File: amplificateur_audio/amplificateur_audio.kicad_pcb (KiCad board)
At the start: 2 copper layers, 54 parts, among them J2 Conn_01x02, J3 Conn_01x03, K1 Relay_1CT, Q1 Q_PNP_EBC, Q10 Q_PNP_BCE, Q11 BC636, Q12 Q_NPN_BCE, Q13 Q_NPN_EBC, Q2 Q_PNP_EBC, Q3 Q_PNP_EBC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

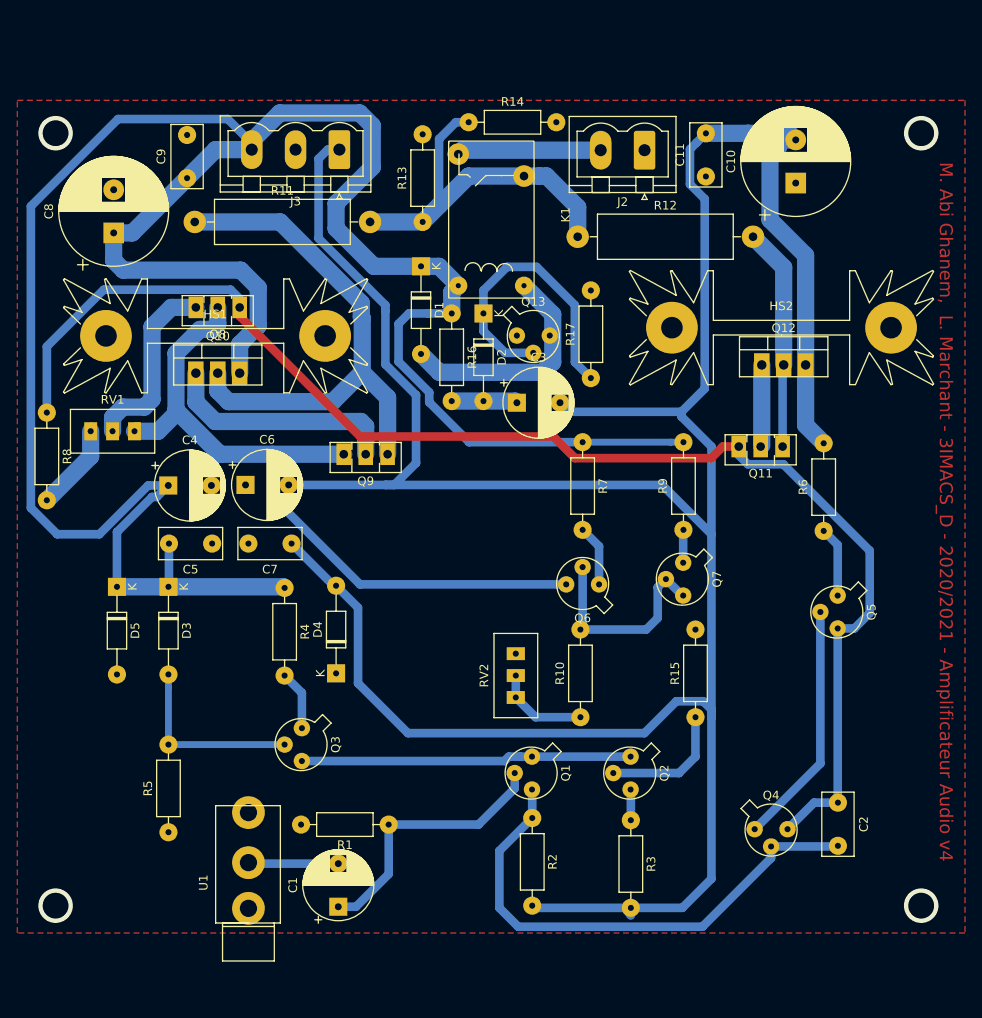
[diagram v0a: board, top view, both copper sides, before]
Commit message: ajout de plan de masse back + vias entre les plans de masses
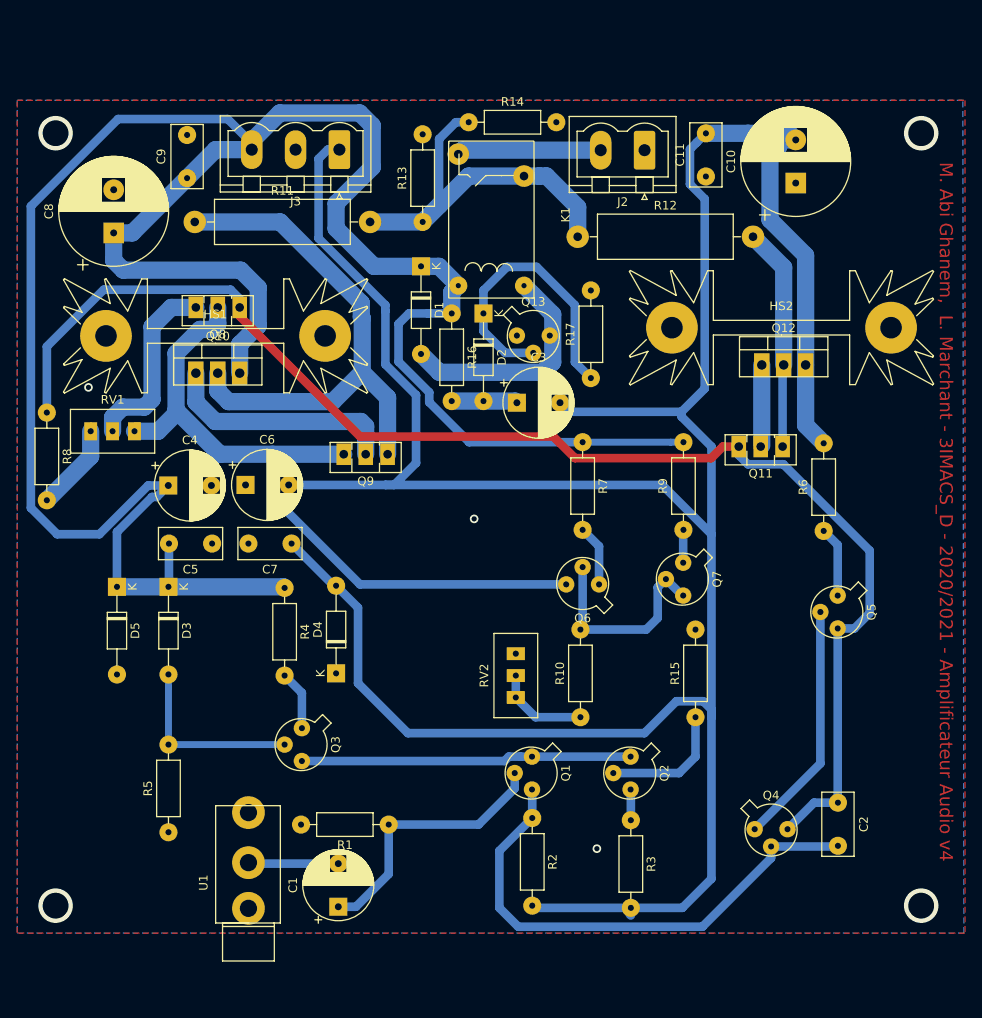
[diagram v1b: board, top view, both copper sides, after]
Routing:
- net GND: vias 0 -> 3
- added copper zone on B.Cu, net GND
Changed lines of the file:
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@@
     (thickness 1.6)
     (drawings 10)
-    (tracks 279)
+    (tracks 282)
     (zones 0)
     (modules 54)
@@
   )
   (setup
-    (last_trace_width 0.7)
+    (last_trace_width 1)
     (user_trace_width 0.8)
     (user_trace_width 1)
@@
   (segment (start 69.064621 99.441) (end 64.1784 94.554779) (width 1) (layer B.Cu) (net 6))
   (segment (start 69.342 99.441) (end 69.064621 99.441) (width 1) (layer B.Cu) (net 6))
+  (via (at 85.344 91.694) (size 1) (drill 0.6) (layers F.Cu B.Cu) (net 7))
+  (via (at 99.568 129.921) (size 1) (drill 0.6) (layers F.Cu B.Cu) (net 7))
+  (via (at 40.64 76.454) (size 1) (drill 0.6) (layers F.Cu B.Cu) (net 7))
   (segment (start 55.372 48.895) (end 52.07 52.197) (width 2) (layer B.Cu) (net 8))
   (segment (start 59.563 48.895) (end 55.372 48.895) (width 2) (layer B.Cu) (net 8))
@@
       )
     )
+  )
+  (zone (net 7) (net_name GND) (layer B.Cu) (hatch edge 0.508)
+    (connect_pads (clearance 0.508))
+    (min_thickness 0.254)
+    (fill yes (arc_segments 16) (thermal_gap 0.508) (thermal_bridge_width 0.508))
+    (polygon
+      (pts
+        (xy 32.385 43.18) (xy 32.385 139.7) (xy 142.113 139.7) (xy 141.986 43.18)
+      )
+    )

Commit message: ampli audio v4 updated DRC
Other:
- rule trace_min: 0.6 -> 0.4
- rule via_min_drill: 0.3 -> 0.6
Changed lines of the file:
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@@
   )
   (setup
-    (last_trace_width 1)
+    (last_trace_width 0.7)
     (user_trace_width 0.8)
     (user_trace_width 1)
@@
     (zone_clearance 0.508)
     (zone_45_only no)
-    (trace_min 0.6)
+    (trace_min 0.4)
     (segment_width 0.2)
     (edge_width 0.15)
@@
     (via_drill 0.6)
     (via_min_size 0.6)
-    (via_min_drill 0.3)
+    (via_min_drill 0.6)
     (user_via 1 0.8)
     (user_via 2 1)
